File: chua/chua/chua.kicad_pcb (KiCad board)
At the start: 2 copper layers, 101.6 x 61 mm, 32 parts, among them J1 AudioJack2, J2 Conn_Coaxial, J3 Conn_01x02_Male, J4 Conn_Coaxial, K1 CONN_3, P1 CONN_1, P2 CONN_1, Q1 2N7000, U1 LM741, U2 LM741, U3 LM741

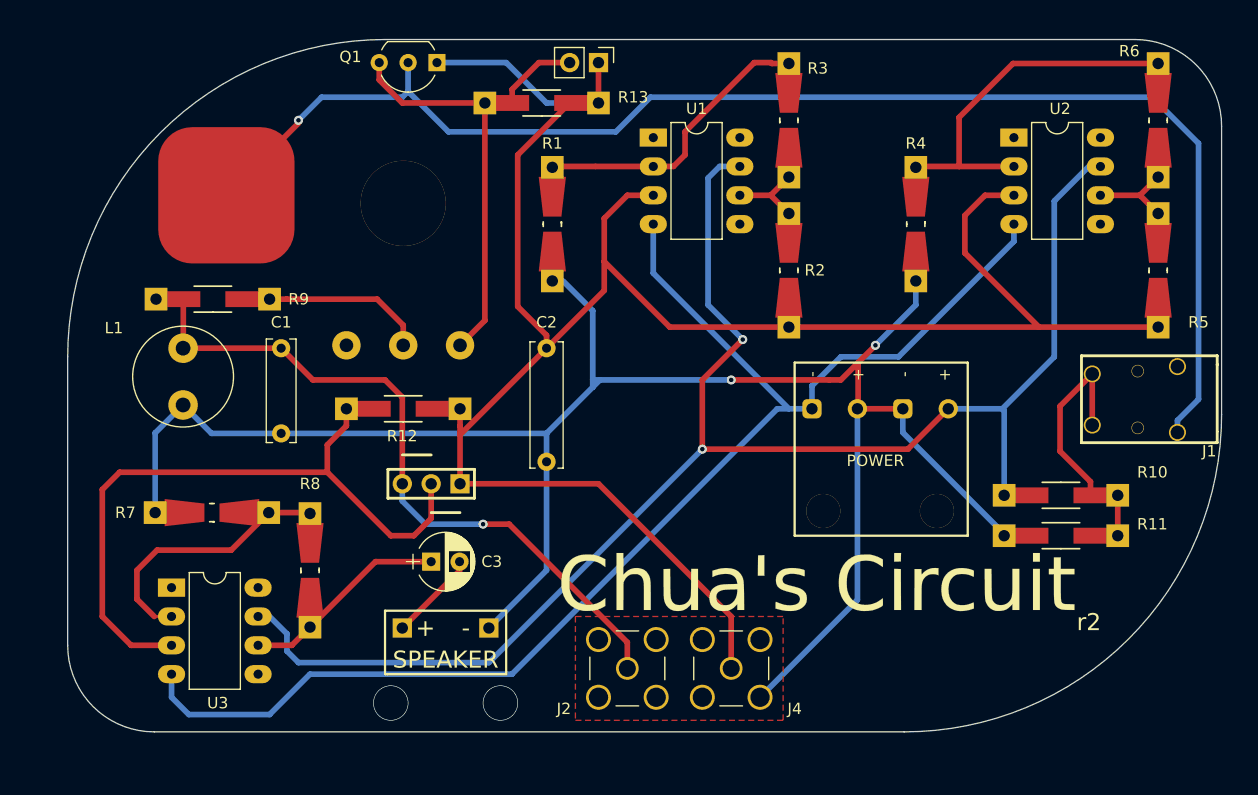
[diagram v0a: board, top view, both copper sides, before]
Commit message: Added new power connector
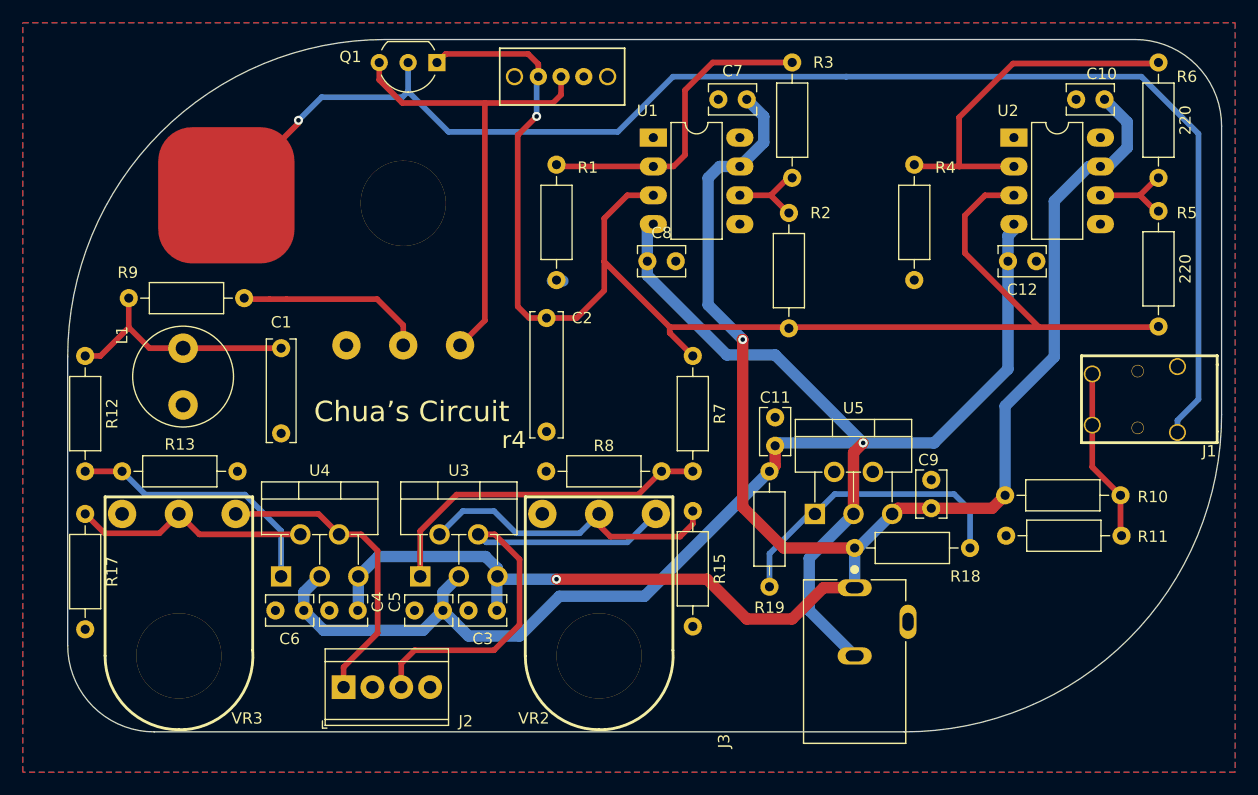
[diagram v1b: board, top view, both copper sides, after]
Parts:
- removed G***: LOGO, chua:chua_text
- removed J4: Conn_Coaxial, Connectors:SMA_THT_Jack_Straight
- removed K1: CONN_3, Socket_Strips:Socket_Strip_Angled_1x03_Pitch2.54mm
- removed P1, P2: CONN_1, Socket_Strips:Socket_Strip_Angled_1x01_Pitch2.54mm
- removed POWER1: Conn_01x04_Male, Socket_Strips:Socket_Strip_Angled_1x04_Pitch2.54mm
- added C10: 100nF, Capacitor_THT:C_Rect_L4.0mm_W2.5mm_P2.50mm, F.Cu at (215.8, 35.8)
- added C11: 100nF, Capacitor_THT:C_Rect_L4.0mm_W2.5mm_P2.50mm, F.Cu at (186.8, 66.2)
- added C12: 100nF, Capacitor_THT:C_Rect_L4.0mm_W2.5mm_P2.50mm, F.Cu at (207.2, 50.0)
- added C4: 100nF, Capacitor_THT:C_Rect_L4.0mm_W2.5mm_P2.50mm, F.Cu at (150.0, 80.8)
- added C5: 100nF, Capacitor_THT:C_Rect_L4.0mm_W2.5mm_P2.50mm, F.Cu at (157.5, 80.8)
- added C6: 100nF, Capacitor_THT:C_Rect_L4.0mm_W2.5mm_P2.50mm, F.Cu at (145.2, 80.8)
- added C7: 100nF, Capacitor_THT:C_Rect_L4.0mm_W2.5mm_P2.50mm, F.Cu at (184.2, 35.8)
- added C8: 100nF, Capacitor_THT:C_Rect_L4.0mm_W2.5mm_P2.50mm, F.Cu at (175.5, 50.0)
- added C9: 100nF, Capacitor_THT:C_Rect_L4.0mm_W2.5mm_P2.50mm, F.Cu at (200.5, 71.8)
- added R15: 180, Resistor_THT:R_Axial_DIN0207_L6.3mm_D2.5mm_P10.16mm_Horizontal, F.Cu at (179.5, 72.0)
- added R17: 180, Resistor_THT:R_Axial_DIN0207_L6.3mm_D2.5mm_P10.16mm_Horizontal, F.Cu at (126.0, 72.2)
- added R18: 1K, Resistor_THT:R_Axial_DIN0207_L6.3mm_D2.5mm_P10.16mm_Horizontal, F.Cu at (193.8, 75.2)
- added R19: 1K, Resistor_THT:R_Axial_DIN0207_L6.3mm_D2.5mm_P10.16mm_Horizontal, F.Cu at (186.2, 78.7)
- added SW1: SW_DPDT_x2, switch:CK_FARN1201430, F.Cu at (168.0, 33.8)
- added U4: lm6500, Package_TO_SOT_THT:TO-220-5_P3.4x3.7mm_StaggerOdd_Lead3.8mm_Vertical, F.Cu at (143.2, 77.8)
- added U5: lm6500, Package_TO_SOT_THT:TO-220-5_P3.4x3.7mm_StaggerOdd_Lead3.8mm_Vertical, F.Cu at (190.2, 72.2)
- added VR2: 1K, VR_B10K:Potentiometer_WirePads_largePads, F.Cu at (176.2, 72.2)
- added VR3: 1/k, VR_B10K:Potentiometer_WirePads_largePads, F.Cu at (139.2, 72.2)
- C3: value C -> 100nF; footprint Capacitors_THT:CP_Radial_D5.0mm_P2.50mm -> Capacitor_THT:C_Rect_L4.0mm_W2.5mm_P2.50mm
- J2: value Conn_Coaxial -> Conn_01x04; footprint Connectors:SMA_THT_Jack_Straight -> TerminalBlock_TE-Connectivity:TerminalBlock_TE_282834-4_1x04_P2.54mm_Horizontal
- J3: value Conn_01x02_Male -> Jack-DC; footprint Socket_Strips:Socket_Strip_Straight_1x02_Pitch2.54mm -> CUI_PJ-102A:CUI_PJ-102A
- R1, R2, R3, R4, R5, R6: footprint Resistors_Universal:Resistor_SMD+THTuniversal_0805to1206_RM10_HandSoldering -> Resistor_THT:R_Axial_DIN0207_L6.3mm_D2.5mm_P10.16mm_Horizontal
- R10: value R -> 200; footprint Resistors_Universal:Resistor_SMD+THTuniversal_1206_RM10_HandSoldering -> Resistor_THT:R_Axial_DIN0207_L6.3mm_D2.5mm_P10.16mm_Horizontal
- R11: value R -> 820; footprint Resistors_Universal:Resistor_SMD+THTuniversal_1206_RM10_HandSoldering -> Resistor_THT:R_Axial_DIN0207_L6.3mm_D2.5mm_P10.16mm_Horizontal
- R12: value R -> 6.8k; footprint Resistors_Universal:Resistor_SMD+THTuniversal_1206_RM10_HandSoldering -> Resistor_THT:R_Axial_DIN0207_L6.3mm_D2.5mm_P10.16mm_Horizontal
- R13: value 0 -> NC; footprint Resistors_Universal:Resistor_SMD+THTuniversal_1206_RM10_HandSoldering -> Resistor_THT:R_Axial_DIN0207_L6.3mm_D2.5mm_P10.16mm_Horizontal
- R7: value R -> 4.2k; footprint Resistors_Universal:Resistor_SMD+THTuniversal_0805to1206_RM10_HandSoldering -> Resistor_THT:R_Axial_DIN0207_L6.3mm_D2.5mm_P10.16mm_Horizontal
- R8: value R -> 4.4k; footprint Resistors_Universal:Resistor_SMD+THTuniversal_0805to1206_RM10_HandSoldering -> Resistor_THT:R_Axial_DIN0207_L6.3mm_D2.5mm_P10.16mm_Horizontal
- R9: value R -> 1K; footprint Resistors_Universal:Resistor_SMD+THTuniversal_1206_RM10_HandSoldering -> Resistor_THT:R_Axial_DIN0207_L6.3mm_D2.5mm_P10.16mm_Horizontal
- U3: value LM741 -> lm6500; footprint Housings_DIP:DIP-8_W7.62mm_LongPads -> Package_TO_SOT_THT:TO-220-5_P3.4x3.7mm_StaggerOdd_Lead3.8mm_Vertical
- VR1: value 1.5K -> 1K; footprint Potentiometers:Potentiometer_WirePads_largePads -> VR_B10K:Potentiometer_WirePads_largePads
- moved J3 57.4 mm to (193.8, 85.2)
- moved R13 49.2 mm to (129.2, 68.5), turned to 0 degrees
- moved R7 44.5 mm to (179.5, 58.3), turned to 270 degrees
- moved R8 32.2 mm to (176.8, 68.5), turned to 180 degrees
- moved R12 28.4 mm to (126.0, 58.3), turned to 270 degrees
- moved J2 25.0 mm to (148.8, 87.5)
- moved U3 21.9 mm to (155.5, 77.8)
- moved C3 7.21 mm to (162.2, 80.8), turned to 180 degrees
- moved R11 5.34 mm to (217.2, 74.2)
- moved R1 5.25 mm to (167.5, 41.5)
- moved R4 5.24 mm to (199.0, 41.5)
- moved R2 5.11 mm to (188.0, 55.9)
- moved R3 5.08 mm to (188.2, 42.7)
- moved R6 5.07 mm to (220.5, 42.7)
- moved R5 4.95 mm to (220.5, 55.8)
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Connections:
- C1 pad 1: Net-(C1-Pad1) -> OUT1
- C2 pad 1: Net-(C2-Pad1) -> OUT2
- C3 pad 1: Net-(C3-Pad1) -> +12V
- C3 pad 2: Net-(C3-Pad2) -> GND
- J2 pad 1: Net-(C1-Pad1) -> POWOUT1
- J3 pad 1: Net-(C2-Pad1) -> +12V
- J3 pad 2: Net-(J3-Pad2) -> -12V
- L1 pad 1: Net-(C1-Pad1) -> OUT1
- Q1 pad 1: Net-(C2-Pad1) -> OUT2
- Q1 pad 3: Net-(J3-Pad2) -> Net-(Q1-Pad3)
- R12 pad 1: Net-(C2-Pad1) -> OUT1
- R12 pad 2: SO -> Net-(R12-Pad2)
- R13 pad 1: Net-(C2-Pad1) -> Net-(R12-Pad2)
- R13 pad 2: Net-(J3-Pad2) -> GND
- R2 pad 1: Net-(C2-Pad1) -> OUT2
- R5 pad 1: Net-(C2-Pad1) -> OUT2
- R7 pad 1: Net-(R7-Pad1) -> OUT2
- R7 pad 2: GND -> Net-(R7-Pad2)
- R8 pad 1: Net-(C3-Pad1) -> Net-(R7-Pad2)
- R8 pad 2: Net-(R7-Pad1) -> GND
- R9 pad 2: Net-(C1-Pad1) -> OUT1
- U1 pad 3: Net-(C2-Pad1) -> OUT2
- U2 pad 3: Net-(C2-Pad1) -> OUT2
- U3 pad 1: Net-(U3-Pad1) -> Net-(R7-Pad2)
- U3 pad 2: Net-(R7-Pad1) -> Net-(R15-Pad1)
- U3 pad 3: SO -> -12V
- U3 pad 4: -12V -> POWOUT2
- U3 pad 5: Net-(U3-Pad5) -> +12V
- VR1 pad 1: Net-(J3-Pad2) -> Net-(Q1-Pad3)
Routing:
- net Net-(C2-Pad1): track 202.9 -> 0.00 mm
- net GND: track 176.5 -> 1.01 mm, vias 2 -> 0
- net OUT2: track 0.00 -> 134.9 mm, vias 0 -> 1
- net Net-(C1-Pad1): track 64.4 -> 0.00 mm, vias 1 -> 0
- net SO: track 62.1 -> 0.00 mm
- net Net-(J3-Pad2): track 43.5 -> 0.00 mm
- net Net-(Q1-Pad3): track 0.00 -> 42.5 mm
- net POWOUT2: track 0.00 -> 41.2 mm
- net Net-(R7-Pad2): track 0.00 -> 30.2 mm
- net Net-(R7-Pad1): track 28.8 -> 0.00 mm
- net -12V: track 120.0 -> 148.0 mm, vias 0 -> 1
- net Net-(R15-Pad1): track 0.00 -> 27.7 mm
- net POWOUT1: track 0.00 -> 27.1 mm
- net Net-(R18-Pad2): track 0.00 -> 26.7 mm
- net +12V: track 142.8 -> 166.4 mm
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- added copper zone on B.Cu, net GND
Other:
- net class power added: clearance 0.2, trace_width 1, via_dia 0.8, via_drill 0.4
- board text added: "Chua’s Circuit"
- board text added: "r4"
- board text removed: "+"
- board text removed: "-"
- board text removed: "SPEAKER"
- board text removed: "r2"
